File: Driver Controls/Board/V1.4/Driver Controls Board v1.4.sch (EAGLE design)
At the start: 22 parts

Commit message: pulldown resistor
added a pulldown resistor to analog pin
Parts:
- added R1: 50K, resistor:R-US_VTA55
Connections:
- new net N$1: R1.2, U$2.A3
- net GND: now also R1.1

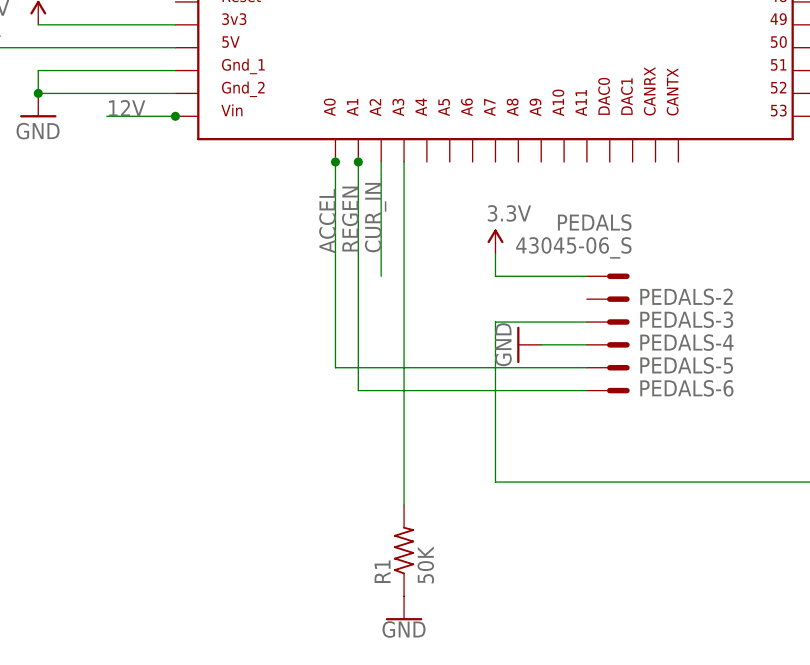
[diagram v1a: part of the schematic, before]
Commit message: driver control board w/ pulldown resistor
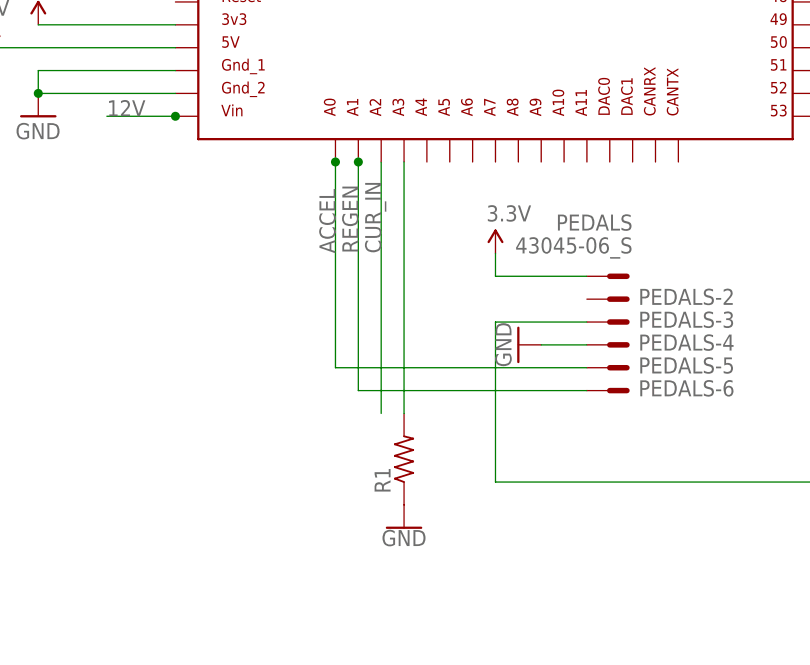
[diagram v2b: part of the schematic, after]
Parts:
- R1: value 50K -> (none); device resistor:R-US_VTA55 -> resistor:R-US_0204/5
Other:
- moved on the sheet: R1
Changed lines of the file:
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@@
 <part name="IGNITION" library="con-molex-mini-fit" deviceset="39-30-?02?_S" device=""/>
 <part name="CAN_CONN_OUT" library="con-molex-mini-fit" deviceset="39-30-?04?" device=""/>
-<part name="R1" library="resistor" library_urn="urn:adsk.eagle:library:348" deviceset="R-US_" device="VTA55" package3d_urn="urn:adsk.eagle:package:26120/2" value="50K"/>
+<part name="R1" library="resistor" library_urn="urn:adsk.eagle:library:348" deviceset="R-US_" device="0204/5" package3d_urn="urn:adsk.eagle:package:23488/1"/>
 <part name="GND4" library="SparkFun-PowerSymbols" deviceset="GND" device=""/>
 </parts>
@@
 <attribute name="VALUE" x="295.91" y="91.44" size="1.778" layer="95"/>
 </instance>
-<instance part="R1" gate="G$1" x="35.56" y="-25.4" smashed="yes" rot="R90">
-<attribute name="NAME" x="34.0614" y="-29.21" size="1.778" layer="95" rot="R90"/>
-<attribute name="VALUE" x="38.862" y="-29.21" size="1.778" layer="96" rot="R90"/>
-</instance>
-<instance part="GND4" gate="1" x="35.56" y="-33.02" smashed="yes">
-<attribute name="VALUE" x="35.56" y="-33.274" size="1.778" layer="96" align="top-center"/>
+<instance part="R1" gate="G$1" x="35.56" y="-15.24" smashed="yes" rot="R90">
+<attribute name="NAME" x="34.0614" y="-19.05" size="1.778" layer="95" rot="R90"/>
+<attribute name="VALUE" x="38.862" y="-19.05" size="1.778" layer="96" rot="R90"/>
+</instance>
+<instance part="GND4" gate="1" x="35.56" y="-22.86" smashed="yes">
+<attribute name="VALUE" x="35.56" y="-23.114" size="1.778" layer="96" align="top-center"/>
 </instance>
 </instances>
@@
 <segment>
 <pinref part="U$2" gate="G$1" pin="A2"/>
-<wire x1="33.02" y1="17.78" x2="33.02" y2="5.08" width="0.1524" layer="91"/>
 <label x="33.02" y="7.62" size="1.778" layer="95" rot="R90"/>
+<wire x1="33.02" y1="17.78" x2="33.02" y2="-10.16" width="0.1524" layer="91"/>
 </segment>
 </net>
@@
 <segment>
 <pinref part="U$2" gate="G$1" pin="A3"/>
-<wire x1="35.56" y1="17.78" x2="35.56" y2="-20.32" width="0.1524" layer="91"/>
+<wire x1="35.56" y1="17.78" x2="35.56" y2="-10.16" width="0.1524" layer="91"/>
 <pinref part="R1" gate="G$1" pin="2"/>
 </segment>
